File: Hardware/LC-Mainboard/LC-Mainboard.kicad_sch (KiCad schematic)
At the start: 15 parts, among them J1 Raspberry_Pi, J2 Charge Controller, U1 MAX3232IDW

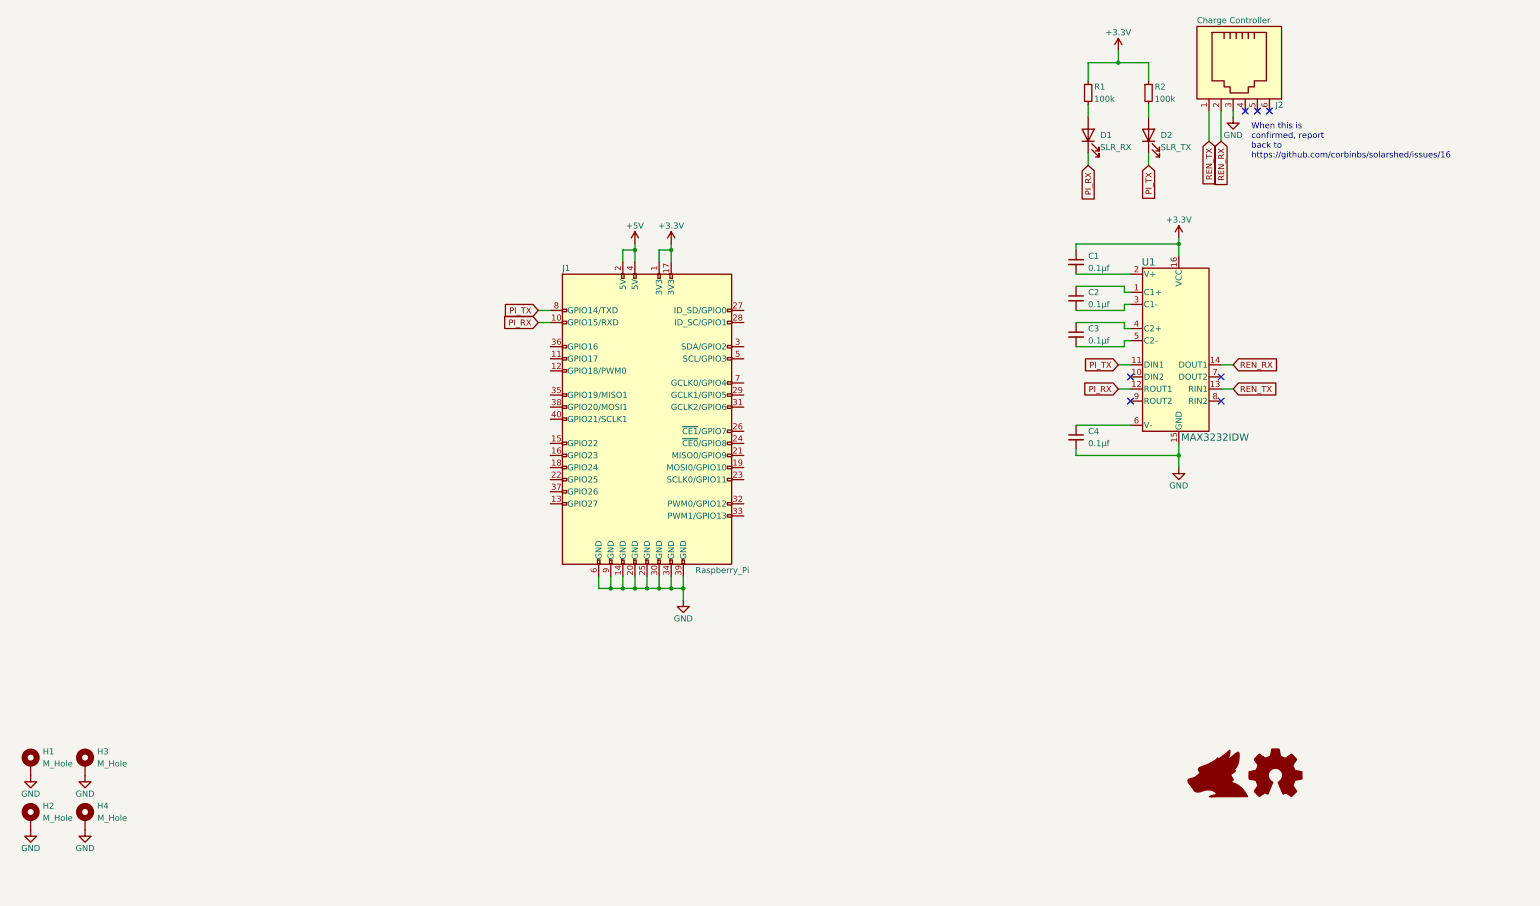
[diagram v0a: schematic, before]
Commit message: bump lib and add LEDs
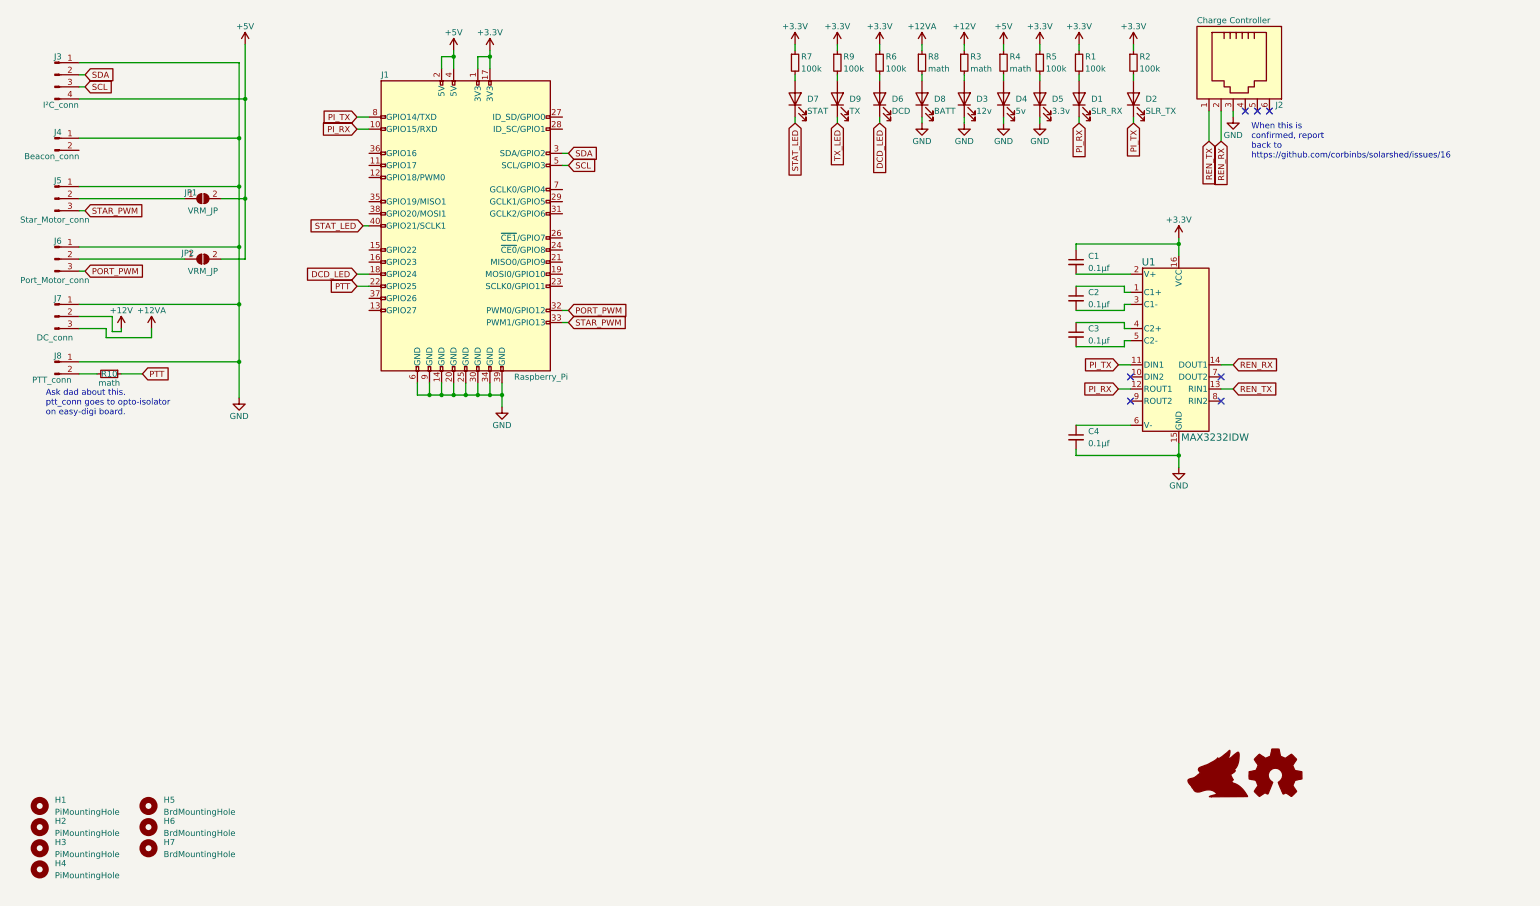
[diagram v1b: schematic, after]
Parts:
- removed H1, H2, H3, H4: M_Hole, MountingHole:MountingHole_3mm_Pad, symbol Mechanical:MountingHole_Pad
- added D3: 12v, LED_SMD:LED_0805_2012Metric, symbol Device:LED
- added D4: 5v, LED_SMD:LED_0805_2012Metric, symbol Device:LED
- added D5: 3.3v, LED_SMD:LED_0805_2012Metric, symbol Device:LED
- added D6: DCD, LED_SMD:LED_0805_2012Metric, symbol Device:LED
- added D7: STAT, LED_SMD:LED_0805_2012Metric, symbol Device:LED
- added D8: BATT, LED_SMD:LED_0805_2012Metric, symbol Device:LED
- added D9: TX, LED_SMD:LED_0805_2012Metric, symbol Device:LED
- added H1, H2, H3, H4: PiMountingHole, MountingHole:MountingHole_3mm, symbol Mechanical:MountingHole
- added H5, H6, H7: BrdMountingHole, MountingHole:MountingHole_3mm, symbol Mechanical:MountingHole
- added J3: I²C_conn, Connector_JST:JST_EH_S4B-EH_1x04_P2.50mm_Horizontal, symbol Connector:Conn_01x04_Male
- added J4: Beacon_conn, Connector_JST:JST_EH_S2B-EH_1x02_P2.50mm_Horizontal, symbol Connector:Conn_01x02_Male
- added J5: Star_Motor_conn, Connector_JST:JST_EH_S3B-EH_1x03_P2.50mm_Horizontal, symbol Connector:Conn_01x03_Male
- added J6: Port_Motor_conn, Connector_JST:JST_EH_S3B-EH_1x03_P2.50mm_Horizontal, symbol Connector:Conn_01x03_Male
- added J7: DC_conn, Connector_JST:JST_EH_S3B-EH_1x03_P2.50mm_Horizontal, symbol Connector:Conn_01x03_Male
- added J8: PTT_conn, Connector_JST:JST_EH_S2B-EH_1x02_P2.50mm_Horizontal, symbol Connector:Conn_01x02_Male
- added JP1, JP2: VRM_JP, Jumper:SolderJumper-2_P1.3mm_Open_Pad1.0x1.5mm, symbol Jumper:SolderJumper_2_Open
- added R10, R3, R4, R8: math, Resistor_SMD:R_0805_2012Metric, symbol Device:R_Small
- added R5, R6, R7, R9: 100k, Resistor_SMD:R_0805_2012Metric, symbol Device:R_Small
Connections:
- net +3V3: now also R5.1, R6.1, R7.1, R9.1
- net +5V: now also J3.4 (Pin_4), JP1.2 (B), JP2.2 (B), R4.1
- net GND: now also D3.1 (K), D4.1 (K), D5.1 (K), D8.1 (K), J3.1 (Pin_1), J4.1 (Pin_1), J5.1 (Pin_1), J6.1 (Pin_1), J7.1 (Pin_1), J8.1 (Pin_1)
- net DCD_LED: now reaches J1.18 (GPIO24)
- net DCD_LED: now also D6.1 (K)
- net PTT: now reaches J1.22 (GPIO25)
- net PTT: now also R10.1
- net SDA: now reaches J1.3 (SDA/GPIO2)
- net SDA: now also J3.2 (Pin_2)
- net PORT_PWM: now reaches J1.32 (PWM0/GPIO12)
- net PORT_PWM: now also J6.3 (Pin_3)
- net STAR_PWM: now reaches J1.33 (PWM1/GPIO13)
- net STAR_PWM: now also J5.3 (Pin_3)
- net STAT_LED: now reaches J1.40 (GPIO21/SCLK1)
- net STAT_LED: now also D7.1 (K)
- net SCL: now reaches J1.5 (SCL/GPIO3)
- net SCL: now also J3.3 (Pin_3)
- new net: D6.2 (A), R6.2
- new net: D7.2 (A), R7.2
- new net: J5.2 (Pin_2), JP1.1 (A)
- new net: J8.2 (Pin_2), R10.2
- new net: D8.2 (A), R8.2
- new net: D9.2 (A), R9.2
- new net: D5.2 (A), R5.2
- new net: D3.2 (A), R3.2
- new net: D4.2 (A), R4.2
- new net: J6.2 (Pin_2), JP2.1 (A)
- new net +12V: J7.2 (Pin_2), R3.1
- new net +12VA: J7.3 (Pin_3), R8.1
- new net TX_LED: D9.1 (K)
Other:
- note added: "Ask dad about this. ptt_conn goes to opto-isolator on easy-digi board."
- moved on the sheet: D1, D2, J1, R1, R2

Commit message: Add a bunch of stuff
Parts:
- added J10, J9: (no value), Connector_JST:JST_EH_S4B-EH_1x04_P2.50mm_Horizontal, symbol Connector:Conn_01x04_Male
- J3: value I²C_conn -> (none)
- J4: value Beacon_conn -> (none)
- J5: value Star_Motor_conn -> (none)
- J6: value Port_Motor_conn -> (none)
- J7: value DC_conn -> (none)
- J8: value PTT_conn -> (none)
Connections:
- net +5V: now also J10.2 (Pin_2), J9.2 (Pin_2)
- net GND: now also J10.1 (Pin_1), J9.1 (Pin_1)
- new net PORT_ENC_A: J10.3 (Pin_3)
- new net PORT_ENC_B: J10.4 (Pin_4)
- new net STAR_ENC_A: J9.3 (Pin_3)
- new net STAR_ENC_B: J9.4 (Pin_4)
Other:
- moved on the sheet: J6, J7, J8, JP2, R10

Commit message: Make a v1.0 hardware release (#2)
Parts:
- removed H5: BrdMountingHole, MountingHole:MountingHole_3mm, symbol Mechanical:MountingHole
- removed J7: (no value), Connector_JST:JST_EH_S3B-EH_1x03_P2.50mm_Horizontal, symbol Connector:Conn_01x03_Male
- added C5, C7: 10μf, Capacitor_SMD:C_Elec_6.3x5.4, symbol Device:C_Small
- added C6: 0.1μf, Capacitor_SMD:C_0805_2012Metric, symbol Device:C_Small
- added J11, J7: (no value), Connector_JST:JST_XH_S2B-XH-A_1x02_P2.50mm_Horizontal, symbol Connector:Conn_01x02_Male
- added Q1: MMBT3906, Package_TO_SOT_SMD:SOT-23, symbol Transistor_BJT:MMBT3906
- added Q2, Q3: MMBT3904, Package_TO_SOT_SMD:SOT-23, symbol Transistor_BJT:MMBT3904
- added R11: 47K, Resistor_SMD:R_0805_2012Metric, symbol Device:R_Small
- added R12, R14, R15: 1K, Resistor_SMD:R_0805_2012Metric, symbol Device:R_Small
- added R13: 47R, Resistor_SMD:R_0805_2012Metric, symbol Device:R_Small
- added U2: NCP1117-12_SOT223, Package_TO_SOT_SMD:SOT-223-3_TabPin2, symbol Regulator_Linear:NCP1117-12_SOT223
- D3: value 12v -> (none)
- D8: value BATT -> (none)
- J10: value (none) -> Port Enc.; footprint Connector_JST:JST_EH_S4B-EH_1x04_P2.50mm_Horizontal -> Connector_JST:JST_XH_S4B-XH-A_1x04_P2.50mm_Horizontal
- J3: value (none) -> I²C; footprint Connector_JST:JST_EH_S4B-EH_1x04_P2.50mm_Horizontal -> Connector_JST:JST_XH_S4B-XH-A_1x04_P2.50mm_Horizontal
- J4: value (none) -> Beacon; footprint Connector_JST:JST_EH_S2B-EH_1x02_P2.50mm_Horizontal -> Connector_JST:JST_XH_S2B-XH-A_1x02_P2.50mm_Horizontal
- J5: value (none) -> Star.Motor; footprint Connector_JST:JST_EH_S3B-EH_1x03_P2.50mm_Horizontal -> Connector_JST:JST_XH_S3B-XH-A_1x03_P2.50mm_Horizontal
- J6: value (none) -> Port Motor; footprint Connector_JST:JST_EH_S3B-EH_1x03_P2.50mm_Horizontal -> Connector_JST:JST_XH_S3B-XH-A_1x03_P2.50mm_Horizontal
- J8: value (none) -> PTT; footprint Connector_JST:JST_EH_S2B-EH_1x02_P2.50mm_Horizontal -> Connector_JST:JST_XH_S2B-XH-A_1x02_P2.50mm_Horizontal
- J9: value (none) -> Star.Enc.; footprint Connector_JST:JST_EH_S4B-EH_1x04_P2.50mm_Horizontal -> Connector_JST:JST_XH_S4B-XH-A_1x04_P2.50mm_Horizontal
- R1, R2, R5, R6, R7, R9: value 100k -> 100R
- R10: value math -> 470R
- R3, R8: value math -> 1K
- R4: value math -> 220R
- renumbered H7 to H5
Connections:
- net TX_LED is gone; now on net PTT: D9.1 (K)
- net +12V: now also C5.1, J7.2 (Pin_2), Q1.2 (E), R11.2, U2.3 (VI)
- net +3V3: now also C7.1; no longer C1.1
- net +5V: now also C6.1, Q3.3 (C), U2.2 (VO)
- net GND: now also C1.2, C5.2, C6.2, C7.2, J11.1 (Pin_1), J7.1 (Pin_1), Q2.2 (E), U2.1 (GND)
- net PORT_ENC_A: now also J1.31 (GCLK2/GPIO6)
- net PORT_ENC_B: now also J1.26 (~{CE1}/GPIO7)
- net STAR_ENC_A: now also J1.7 (GCLK0/GPIO4)
- net STAR_ENC_B: now also J1.29 (GCLK1/GPIO5)
- net at U1.2 (V+): now also C1.1; no longer C1.2
- net BCON_LOAD: now reaches J4.2 (Pin_2)
- net BCON_LOAD: now also R13.1
- net LOAD_EN_Pi: now reaches J1.21 (MISO0/GPIO9)
- net LOAD_EN_Pi: now also R15.2
- net BCON_LED: now reaches J1.38 (GPIO20/MOSI1)
- net BCON_LED: now also R14.1
- net +12VA renamed LOAD_EN
- net LOAD_EN: now also J11.2 (Pin_2), Q3.2 (E)
- new net: Q1.1 (B), R11.1, R12.2
- new net: Q1.3 (C), R13.2
- new net: Q3.1 (B), R15.1
- new net: Q2.1 (B), R14.2
- new net: Q2.3 (C), R12.1
- no-connect marks 7 -> 20
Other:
- note added: "47ohm half watt works as fuse"
- note added: "This chip may be fine for the pi3 (less than 1A) but the pi4 can use up to 2A"
- note removed: "Ask dad about this. ptt_conn goes to opto-isolator on easy-digi board."
- moved on the sheet: C1, D3, D4, D6, D7, D8, D9, H5, J8, JP1, JP2, R10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

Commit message: Bump
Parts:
- D3: value (none) -> BATT
- D8: value (none) -> LOAD
- J11: value (none) -> Load En.
- J7: value (none) -> DC In
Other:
- moved on the sheet: C7
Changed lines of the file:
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@@
     (stroke (width 0) (type default) (color 0 0 0 0))
   )
-  (wire (pts (xy 268.605 62.865) (xy 268.605 64.135))
+  (wire (pts (xy 273.05 62.865) (xy 273.05 64.135))
     (stroke (width 0) (type default) (color 0 0 0 0))
   )
@@
     (stroke (width 0) (type default) (color 0 0 0 0))
   )
-  (wire (pts (xy 268.605 70.485) (xy 268.605 69.215))
+  (wire (pts (xy 273.05 70.485) (xy 273.05 69.215))
     (stroke (width 0) (type default) (color 0 0 0 0))
   )
@@
     (pin "2")
   )
-  (symbol (lib_id "Device:C_Small") (at 268.605 66.675 0) (unit 1)
-    (in_bom yes) (on_board yes)
-    (property "Reference" "C7" (id 0) (at 270.51 65.405 0)
-      (effects (font (size 1.27 1.27)) (justify left))
-    )
-    (property "Value" "10μf" (id 1) (at 270.51 67.945 0)
-      (effects (font (size 1.27 1.27)) (justify left))
-    )
-    (property "Footprint" "Capacitor_SMD:C_Elec_6.3x5.4" (id 2) (at 268.605 66.675 0)
-      (effects (font (size 1.27 1.27)) hide)
-    )
-    (property "Datasheet" "~" (id 3) (at 268.605 66.675 0)
+  (symbol (lib_id "Device:C_Small") (at 273.05 66.675 0) (unit 1)
+    (in_bom yes) (on_board yes)
+    (property "Reference" "C7" (id 0) (at 274.955 65.405 0)
+      (effects (font (size 1.27 1.27)) (justify left))
+    )
+    (property "Value" "10μf" (id 1) (at 274.955 67.945 0)
+      (effects (font (size 1.27 1.27)) (justify left))
+    )
+    (property "Footprint" "Capacitor_SMD:C_Elec_6.3x5.4" (id 2) (at 273.05 66.675 0)
+      (effects (font (size 1.27 1.27)) hide)
+    )
+    (property "Datasheet" "~" (id 3) (at 273.05 66.675 0)
       (effects (font (size 1.27 1.27)) hide)
     )
@@
     (pin "1")
   )
-  (symbol (lib_id "power:GND") (at 268.605 70.485 0) (unit 1)
-    (in_bom yes) (on_board yes)
-    (property "Reference" "#PWR0136" (id 0) (at 268.605 76.835 0)
-      (effects (font (size 1.27 1.27)) hide)
-    )
-    (property "Value" "GND" (id 1) (at 268.605 74.295 0))
-    (property "Footprint" "" (id 2) (at 268.605 70.485 0)
-      (effects (font (size 1.27 1.27)) hide)
-    )
-    (property "Datasheet" "" (id 3) (at 268.605 70.485 0)
+  (symbol (lib_id "power:GND") (at 273.05 70.485 0) (unit 1)
+    (in_bom yes) (on_board yes)
+    (property "Reference" "#PWR0136" (id 0) (at 273.05 76.835 0)
+      (effects (font (size 1.27 1.27)) hide)
+    )
+    (property "Value" "GND" (id 1) (at 273.05 74.295 0))
+    (property "Footprint" "" (id 2) (at 273.05 70.485 0)
+      (effects (font (size 1.27 1.27)) hide)
+    )
+    (property "Datasheet" "" (id 3) (at 273.05 70.485 0)
       (effects (font (size 1.27 1.27)) hide)
     )
@@
     (in_bom yes) (on_board yes)
     (property "Reference" "J11" (id 0) (at 22.225 118.745 0))
-    (property "Value" "" (id 1) (at 20.32 123.825 0))
+    (property "Value" "Load En." (id 1) (at 20.32 123.825 0))
     (property "Footprint" "Connector_JST:JST_XH_S2B-XH-A_1x02_P2.50mm_Horizontal" (id 2) (at 21.59 120.015 0)
       (effects (font (size 1.27 1.27)) hide)
@@
     (pin "1")
   )
-  (symbol (lib_id "power:+3.3V") (at 268.605 62.865 0) (unit 1)
-    (in_bom yes) (on_board yes)
-    (property "Reference" "#PWR0135" (id 0) (at 268.605 66.675 0)
-      (effects (font (size 1.27 1.27)) hide)
-    )
-    (property "Value" "+3.3V" (id 1) (at 268.605 59.055 0))
-    (property "Footprint" "" (id 2) (at 268.605 62.865 0)
-      (effects (font (size 1.27 1.27)) hide)
-    )
-    (property "Datasheet" "" (id 3) (at 268.605 62.865 0)
+  (symbol (lib_id "power:+3.3V") (at 273.05 62.865 0) (unit 1)
+    (in_bom yes) (on_board yes)
+    (property "Reference" "#PWR0135" (id 0) (at 273.05 66.675 0)
+      (effects (font (size 1.27 1.27)) hide)
+    )
+    (property "Value" "+3.3V" (id 1) (at 273.05 59.055 0))
+    (property "Footprint" "" (id 2) (at 273.05 62.865 0)
+      (effects (font (size 1.27 1.27)) hide)
+    )
+    (property "Datasheet" "" (id 3) (at 273.05 62.865 0)
       (effects (font (size 1.27 1.27)) hide)
     )
@@
       (effects (font (size 1.27 1.27)) (justify right))
     )
-    (property "Value" "" (id 1) (at 177.165 38.1 90)
+    (property "Value" "LOAD" (id 1) (at 177.165 38.1 90)
       (effects (font (size 1.27 1.27)) (justify right))
     )
@@
     (in_bom yes) (on_board yes)
     (property "Reference" "J7" (id 0) (at 22.225 101.6 0))
-    (property "Value" "" (id 1) (at 22.225 106.68 0))
+    (property "Value" "DC In" (id 1) (at 22.225 106.68 0))
     (property "Footprint" "Connector_JST:JST_XH_S2B-XH-A_1x02_P2.50mm_Horizontal" (id 2) (at 21.59 102.87 0)
       (effects (font (size 1.27 1.27)) hide)
@@
       (effects (font (size 1.27 1.27)) hide)
     )
-    (property "Value" "" (id 1) (at 104.14 106.045 0))
+    (property "Value" "+5V" (id 1) (at 104.14 106.045 0))
     (property "Footprint" "" (id 2) (at 104.14 109.855 0)
       (effects (font (size 1.27 1.27)) hide)
@@
       (effects (font (size 1.27 1.27)) (justify right))
     )
-    (property "Value" "" (id 1) (at 187.96 33.02 90)
+    (property "Value" "BATT" (id 1) (at 187.96 33.02 90)
       (effects (font (size 1.27 1.27)) (justify right))
     )

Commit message: Replace caps with the right sized ones
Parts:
- C5, C7: footprint Capacitor_SMD:C_Elec_6.3x5.4 -> Capacitor_SMD:C_Elec_4x5.4
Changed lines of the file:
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@@
       (effects (font (size 1.27 1.27)) (justify left))
     )
-    (property "Footprint" "Capacitor_SMD:C_Elec_6.3x5.4" (id 2) (at 28.575 152.4 0)
+    (property "Footprint" "Capacitor_SMD:C_Elec_4x5.4" (id 2) (at 28.575 152.4 0)
       (effects (font (size 1.27 1.27)) hide)
     )
@@
       (effects (font (size 1.27 1.27)) (justify left))
     )
-    (property "Footprint" "Capacitor_SMD:C_Elec_6.3x5.4" (id 2) (at 273.05 66.675 0)
+    (property "Footprint" "Capacitor_SMD:C_Elec_4x5.4" (id 2) (at 273.05 66.675 0)
       (effects (font (size 1.27 1.27)) hide)
     )
@@
     )
     (path "/01c4ca08-8a4f-4fcc-ac99-649d9d9accf3"
-      (reference "C5") (unit 1) (value "10μf") (footprint "Capacitor_SMD:C_Elec_6.3x5.4")
+      (reference "C5") (unit 1) (value "10μf") (footprint "Capacitor_SMD:C_Elec_4x5.4")
     )
     (path "/7980da57-e531-4bfc-96c3-7b523e53653f"
@@
     )
     (path "/02f7cd38-e80c-4cea-990c-b710e96f02a9"
-      (reference "C7") (unit 1) (value "10μf") (footprint "Capacitor_SMD:C_Elec_6.3x5.4")
+      (reference "C7") (unit 1) (value "10μf") (footprint "Capacitor_SMD:C_Elec_4x5.4")
     )
     (path "/9b52dbe1-88ca-4ae1-a70d-e55e71d1adec"
